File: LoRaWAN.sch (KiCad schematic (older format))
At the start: 4 parts, among them U3 RFM9xW

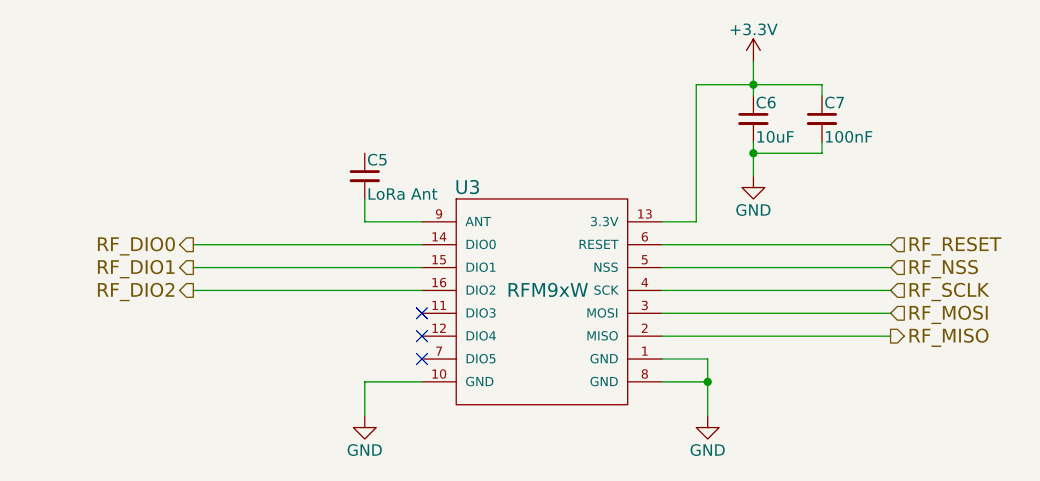
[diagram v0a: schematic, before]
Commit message: Added edge-mount SMAs
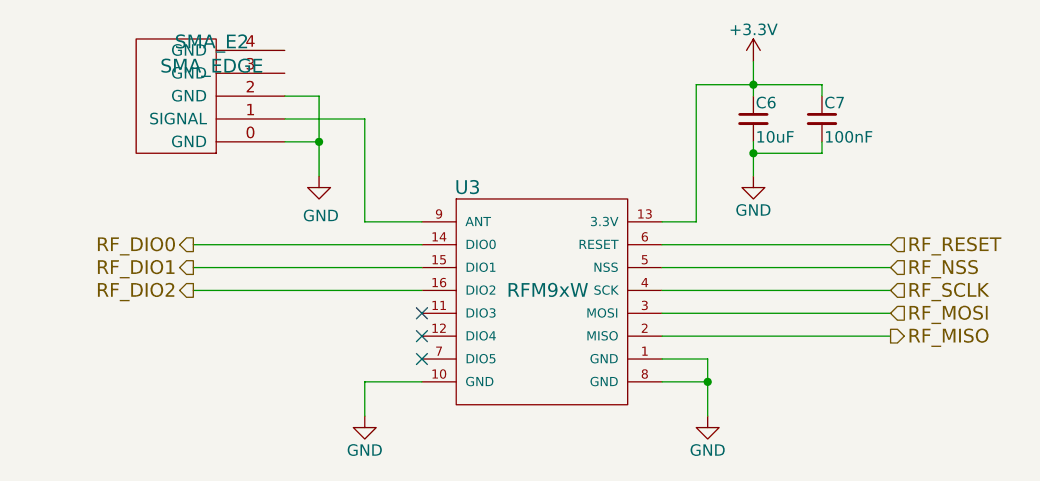
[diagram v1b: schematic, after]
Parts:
- removed C5: LoRa Ant, SMA, symbol C_Small
- added SMA_E2: SMA_EDGE, SMA_EDGE:SMA_EDGE, symbol SMA_EDGE
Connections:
- net GND: now also SMA_E2.0 (GND), SMA_E2.2 (GND)
- net at U3.9 (ANT): now also SMA_E2.1 (SIGNAL)
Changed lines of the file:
@@
 LIBS:miniultrapro
 LIBS:texas-instruments
+LIBS:sma_edge
 LIBS:lorawan_gps-cache
 EELAYER 25 0
@@
 	1    0    0    -1
 $EndComp
-Wire Wire Line
-	6150 3500 6350 3500
-Wire Wire Line
-	6350 3500 6350 3750
-Wire Wire Line
-	6150 3600 6350 3600
-Connection ~ 6350 3600
-Wire Wire Line
-	4850 3750 4850 3600
-Wire Wire Line
-	4850 3600 5100 3600
 $Comp
 L +3.3V #PWR010
@@
 	1    0    0    -1
 $EndComp
+$Comp
+L GND #PWR011
+U 1 1 56EAE25E
+P 6550 2700
+F 0 "#PWR011" H 6550 2450 50  0001 C CNN
+F 1 "GND" H 6550 2550 50  0000 C CNN
+F 2 "" H 6550 2700 50  0000 C CNN
+F 3 "" H 6550 2700 50  0000 C CNN
+	1    6550 2700
+	1    0    0    -1
+$EndComp
+Text HLabel 7150 3000 2    60   Input ~ 0
+RF_RESET
+Text HLabel 7150 3100 2    60   Input ~ 0
+RF_NSS
+Text HLabel 7150 3200 2    60   Input ~ 0
+RF_SCLK
+Text HLabel 7150 3300 2    60   Input ~ 0
+RF_MOSI
+Text HLabel 7150 3400 2    60   Output ~ 0
+RF_MISO
+Text HLabel 4100 3000 0    60   Output ~ 0
+RF_DIO0
+Text HLabel 4100 3100 0    60   Output ~ 0
+RF_DIO1
+Text HLabel 4100 3200 0    60   Output ~ 0
+RF_DIO2
+$Comp
+L SMA_EDGE SMA_E2
+U 1 1 56F512D1
+P 4150 2450
+F 0 "SMA_E2" H 4119 2113 60  0000 C CNN
+F 1 "SMA_EDGE" H 4119 2219 60  0000 C CNN
+F 2 "SMA_EDGE:SMA_EDGE" H 4150 2450 60  0001 C CNN
+F 3 "" H 4150 2450 60  0000 C CNN
+	1    4150 2450
+	-1   0    0    1
+$EndComp
+$Comp
+L GND #PWR012
+U 1 1 56F51345
+P 4650 2700
+F 0 "#PWR012" H 4650 2450 50  0001 C CNN
+F 1 "GND" H 4658 2526 50  0000 C CNN
+F 2 "" H 4650 2700 50  0000 C CNN
+F 3 "" H 4650 2700 50  0000 C CNN
+	1    4650 2700
+	1    0    0    -1
+$EndComp
+Wire Wire Line
+	6150 3500 6350 3500
+Wire Wire Line
+	6350 3500 6350 3750
+Wire Wire Line
+	6150 3600 6350 3600
+Connection ~ 6350 3600
+Wire Wire Line
+	4850 3750 4850 3600
+Wire Wire Line
+	4850 3600 5100 3600
 Wire Wire Line
 	6150 2900 6300 2900
@@
 	6550 2200 6550 2350
 Connection ~ 6550 2300
-$Comp
-L GND #PWR011
-U 1 1 56EAE25E
-P 6550 2700
-F 0 "#PWR011" H 6550 2450 50  0001 C CNN
-F 1 "GND" H 6550 2550 50  0000 C CNN
-F 2 "" H 6550 2700 50  0000 C CNN
-F 3 "" H 6550 2700 50  0000 C CNN
-	1    6550 2700
-	1    0    0    -1
-$EndComp
 Wire Wire Line
 	6550 2700 6550 2550
@@
 Wire Wire Line
 	5100 3200 4100 3200
-Text HLabel 7150 3000 2    60   Input ~ 0
-RF_RESET
-Text HLabel 7150 3100 2    60   Input ~ 0
-RF_NSS
-Text HLabel 7150 3200 2    60   Input ~ 0
-RF_SCLK
-Text HLabel 7150 3300 2    60   Input ~ 0
-RF_MOSI
-Text HLabel 7150 3400 2    60   Output ~ 0
-RF_MISO
-Text HLabel 4100 3000 0    60   Output ~ 0
-RF_DIO0
-Text HLabel 4100 3100 0    60   Output ~ 0
-RF_DIO1
-Text HLabel 4100 3200 0    60   Output ~ 0
-RF_DIO2
-$Comp
-L C_Small C5
-U 1 1 56EBF9F4
-P 4850 2700
-F 0 "C5" H 4860 2770 50  0000 L CNN
-F 1 "LoRa Ant" H 4860 2620 50  0000 L CNN
-F 2 "SMA" H 4850 2700 50  0001 C CNN
-F 3 "" H 4850 2700 50  0000 C CNN
-	1    4850 2700
-	1    0    0    -1
-$EndComp
 Wire Wire Line
 	4850 2900 5100 2900
 Wire Wire Line
-	4850 2900 4850 2800
+	4850 2450 4850 2900
+Wire Wire Line
+	4850 2450 4500 2450
+Wire Wire Line
+	4500 2350 4650 2350
+Wire Wire Line
+	4650 2350 4650 2700
+Wire Wire Line
+	4500 2550 4650 2550
+Connection ~ 4650 2550
 $EndSCHEMATC

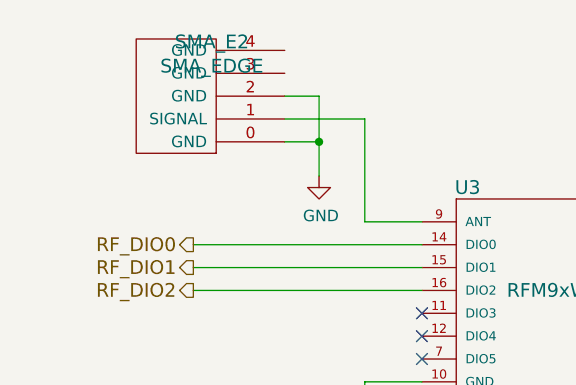
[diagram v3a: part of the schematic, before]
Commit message: Started changes after first round, micro usb connector, fixing footprint for accelerometer
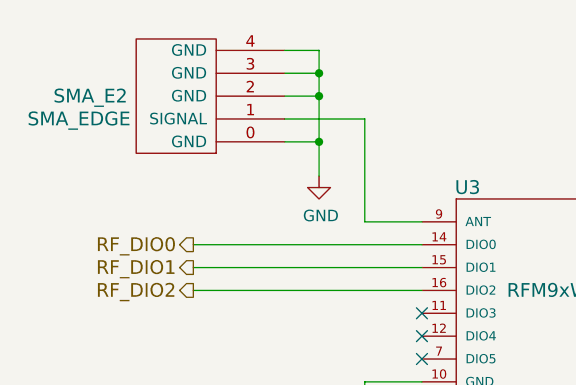
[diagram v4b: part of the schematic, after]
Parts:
- SMA_E2: footprint SMA_EDGE:SMA_EDGE -> edgemount_sma:SMA_EDGE
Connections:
- net GND: now also SMA_E2.3 (GND), SMA_E2.4 (GND)
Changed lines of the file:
@@
 U 1 1 56F512D1
 P 4150 2450
-F 0 "SMA_E2" H 4119 2113 60  0000 C CNN
-F 1 "SMA_EDGE" H 4119 2219 60  0000 C CNN
-F 2 "SMA_EDGE:SMA_EDGE" H 4150 2450 60  0001 C CNN
+F 0 "SMA_E2" H 4650 2350 60  0000 C CNN
+F 1 "SMA_EDGE" H 4700 2450 60  0000 C CNN
+F 2 "edgemount_sma:SMA_EDGE" H 4150 2450 60  0001 C CNN
 F 3 "" H 4150 2450 60  0000 C CNN
 	1    4150 2450
@@
 	4500 2350 4650 2350
 Wire Wire Line
-	4650 2350 4650 2700
+	4650 2150 4650 2700
 Wire Wire Line
 	4500 2550 4650 2550
 Connection ~ 4650 2550
+Wire Wire Line
+	4500 2150 4650 2150
+Connection ~ 4650 2350
+Wire Wire Line
+	4500 2250 4650 2250
+Connection ~ 4650 2250
 $EndSCHEMATC

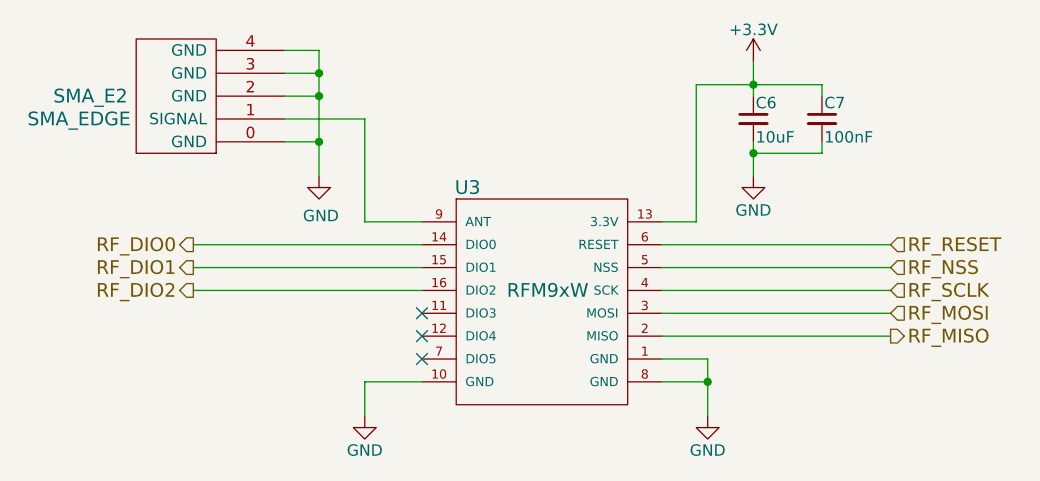
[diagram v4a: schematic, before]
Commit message: Added dielectric antennae, finished wiring, DRC pass, no unconnects
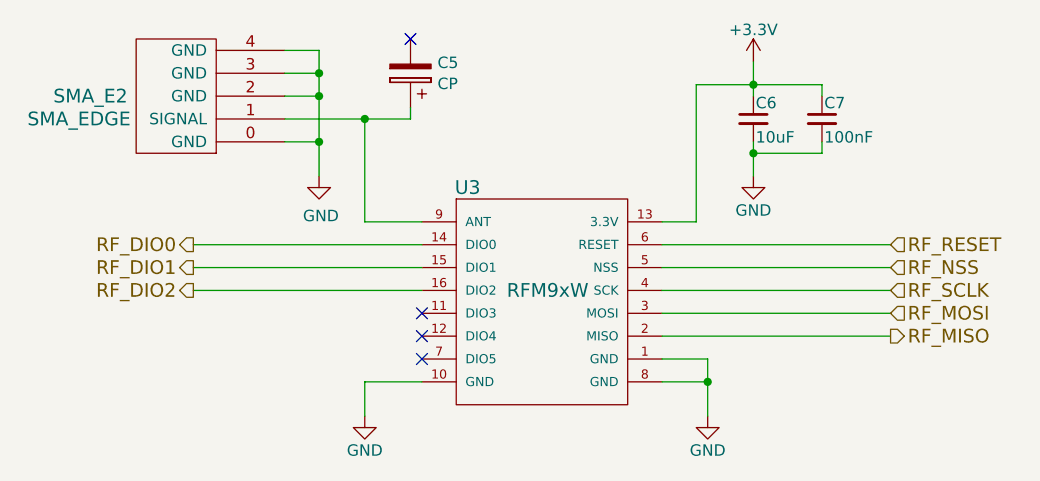
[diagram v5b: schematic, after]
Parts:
- added C5: CP, Johanson:0868AT43A0020, symbol CP
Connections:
- net at SMA_E2.1 (SIGNAL), U3.9 (ANT): now also C5.1
- no-connect marks 3 -> 4
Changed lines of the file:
@@
 	4850 2450 4850 2900
 Wire Wire Line
-	4850 2450 4500 2450
+	4500 2450 5050 2450
 Wire Wire Line
 	4500 2350 4650 2350
@@
 	4500 2250 4650 2250
 Connection ~ 4650 2250
+$Comp
+L CP C5
+U 1 1 573143AB
+P 5050 2250
+F 0 "C5" H 4932 2204 50  0000 R CNN
+F 1 "CP" H 4932 2296 50  0000 R CNN
+F 2 "Johanson:0868AT43A0020" H 5088 2100 50  0001 C CNN
+F 3 "" H 5050 2250 50  0000 C CNN
+F 4 "Johanson" H 5050 2250 60  0001 C CNN "MFG Name"
+F 5 "0868AT43A0020" H 5050 2250 60  0001 C CNN "MFG Part Number"
+	1    5050 2250
+	-1   0    0    1
+$EndComp
+Wire Wire Line
+	5050 2450 5050 2400
+Connection ~ 4850 2450
+NoConn ~ 5050 2100
 $EndSCHEMATC
